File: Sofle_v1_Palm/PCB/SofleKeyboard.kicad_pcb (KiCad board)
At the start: 2 copper layers, 137.2 x 109.2 mm, 85 parts, among them J1 LED, J2 4PIN, J3 OLED, P1 i2c_pin, P2 i2c_pin, SW1 SW_PUSH, SW10 SW_PUSH, SW11 SW_PUSH, SW12 SW_PUSH, SW13 SW_PUSH, SW14 SW_PUSH, SW15 SW_PUSH, SW16 SW_PUSH, SW17 SW_PUSH, SW18 SW_PUSH, SW19 SW_PUSH, SW2 SW_PUSH, SW20 SW_PUSH, SW21 SW_PUSH, SW22 SW_PUSH, SW23 SW_PUSH, SW24 SW_PUSH, SW25 Rotary_Encoder_Switch, SW26 SW_PUSH, SW27 SW_PUSH, SW28 SW_PUSH, SW29 SW_PUSH, SW3 SW_PUSH, SW30 SW_PUSH, SW4 SW_PUSH, SW5 SW_PUSH, SW6 SW_PUSH, SW7 SW_PUSH, SW8 SW_PUSH, SW9 SW_PUSH, U1 ProMicro

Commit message: Re-release of the gerber file with KiCad V5.
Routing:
- net GND: vias 46 -> 45
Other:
- rule pad_to_mask_clearance: 0.2 -> 0

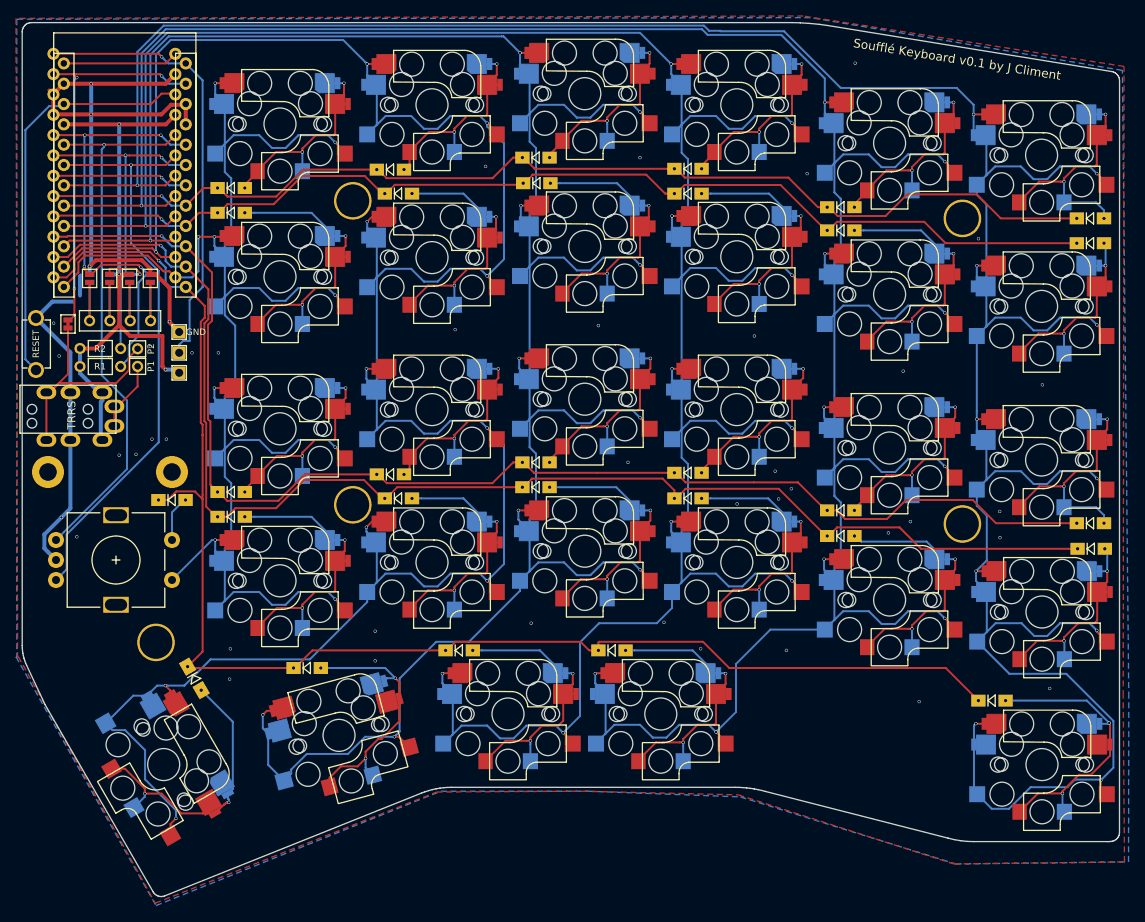
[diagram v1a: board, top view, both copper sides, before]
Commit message: Added top and lower case PCB files.
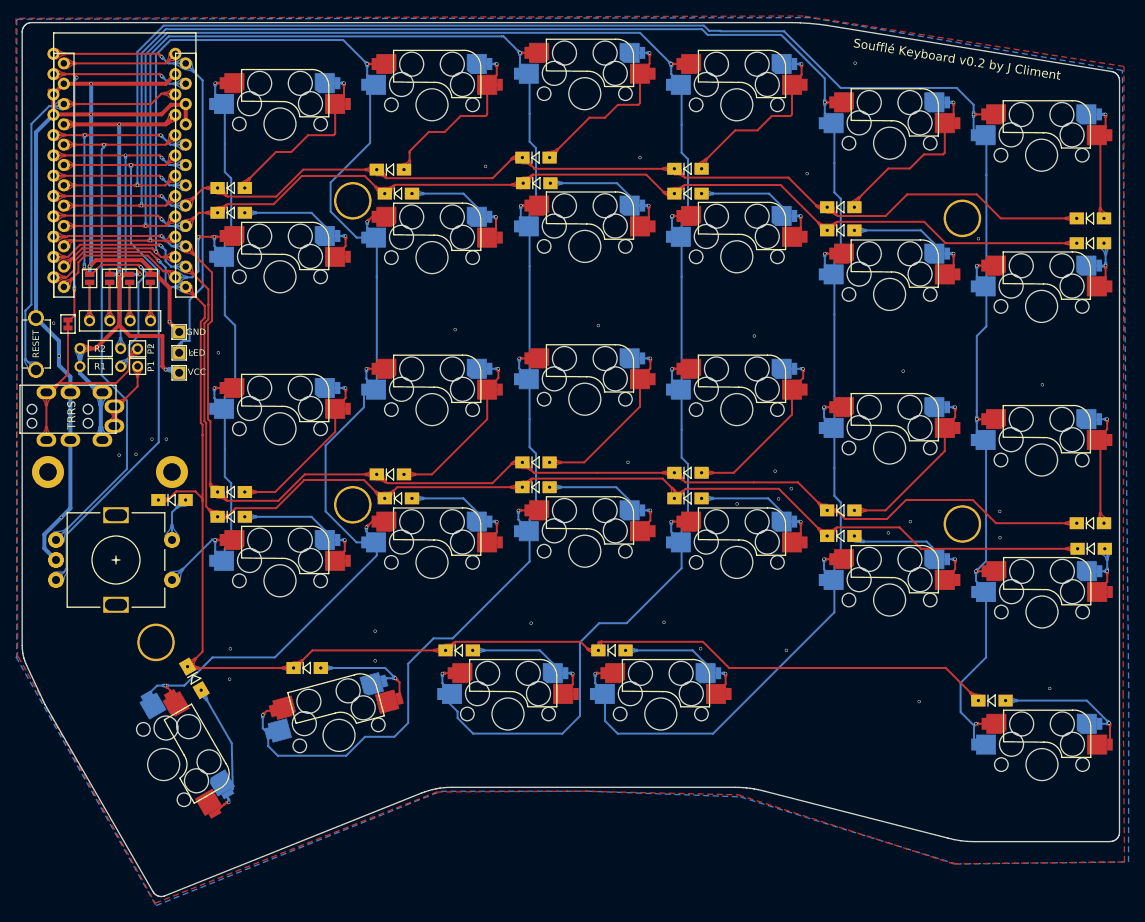
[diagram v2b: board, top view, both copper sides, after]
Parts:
- SW1, SW10, SW11, SW12, SW13, SW14, SW15, SW16, SW17, SW18, SW19, SW2, SW20, SW21, SW22, SW23, SW24, SW27, SW28, SW29, SW3, SW30, SW4, SW5, SW6, SW7, SW8, SW9: footprint SofleKeyboard-footprint:CherryMX_KailhLowProfile_Hotswap -> SofleKeyboard-footprint:CherryMX_Hotswap_mod
- SW26: footprint SofleKeyboard-footprint:CherryMX_KailhLowProfile_Hotswap_1.5 -> SofleKeyboard-footprint:CherryMX_Hotswap_1.5_mod
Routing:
- net col0: track 363.9 -> 246.9 mm, vias 11 -> 6
- net col4: track 311.0 -> 202.1 mm, vias 11 -> 6
- net col1: track 350.6 -> 263.6 mm, vias 11 -> 6
- net col2: track 334.4 -> 249.1 mm, vias 11 -> 6
- net col3: track 314.7 -> 230.3 mm, vias 11 -> 6
- net SW25A: track 206.1 -> 122.8 mm, vias 9 -> 5
- net Net-(D27-Pad2): track 32.8 -> 14.2 mm, vias 2 -> 1
- net Net-(D26-Pad2): track 36.4 -> 17.9 mm, vias 2 -> 1
- net GND: track 124.4 -> 142.7 mm
- net Net-(D30-Pad2): track 36.2 -> 18.1 mm, vias 2 -> 1
- net Net-(D19-Pad2): track 37.2 -> 19.1 mm, vias 2 -> 1
- net Net-(D12-Pad2): track 28.0 -> 9.92 mm, vias 2 -> 1
- net Net-(D9-Pad2): track 36.9 -> 18.8 mm, vias 2 -> 1
- net Net-(D22-Pad2): track 37.1 -> 19.0 mm, vias 2 -> 1
- net Net-(D11-Pad2): track 37.1 -> 19.0 mm, vias 2 -> 1
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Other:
- net class Default removed
- net class GND removed
- net class VCC removed
- board text added: "Soufflé Keyboard v0.2 by J Climent"
- board text removed: "Soufflé Keyboard v0.1 by J Climent"

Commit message: Checkpoint commit.
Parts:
- moved W1 0.28 mm to (93.7, 74.9)
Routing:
- net col2: track 249.1 -> 250.6 mm
- net Net-(D2-Pad2): track 25.1 -> 23.7 mm
- net col1: track 263.6 -> 264.5 mm
- net col3: track 230.3 -> 231.0 mm
- net Net-(D4-Pad2): track 25.4 -> 24.7 mm
- net Net-(D1-Pad2): track 25.2 -> 24.6 mm
- net Net-(D5-Pad2): track 25.2 -> 24.7 mm
- net GND: vias 45 -> 74
